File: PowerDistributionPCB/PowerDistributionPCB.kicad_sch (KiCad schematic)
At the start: 23 parts, among them J1 USB3_A

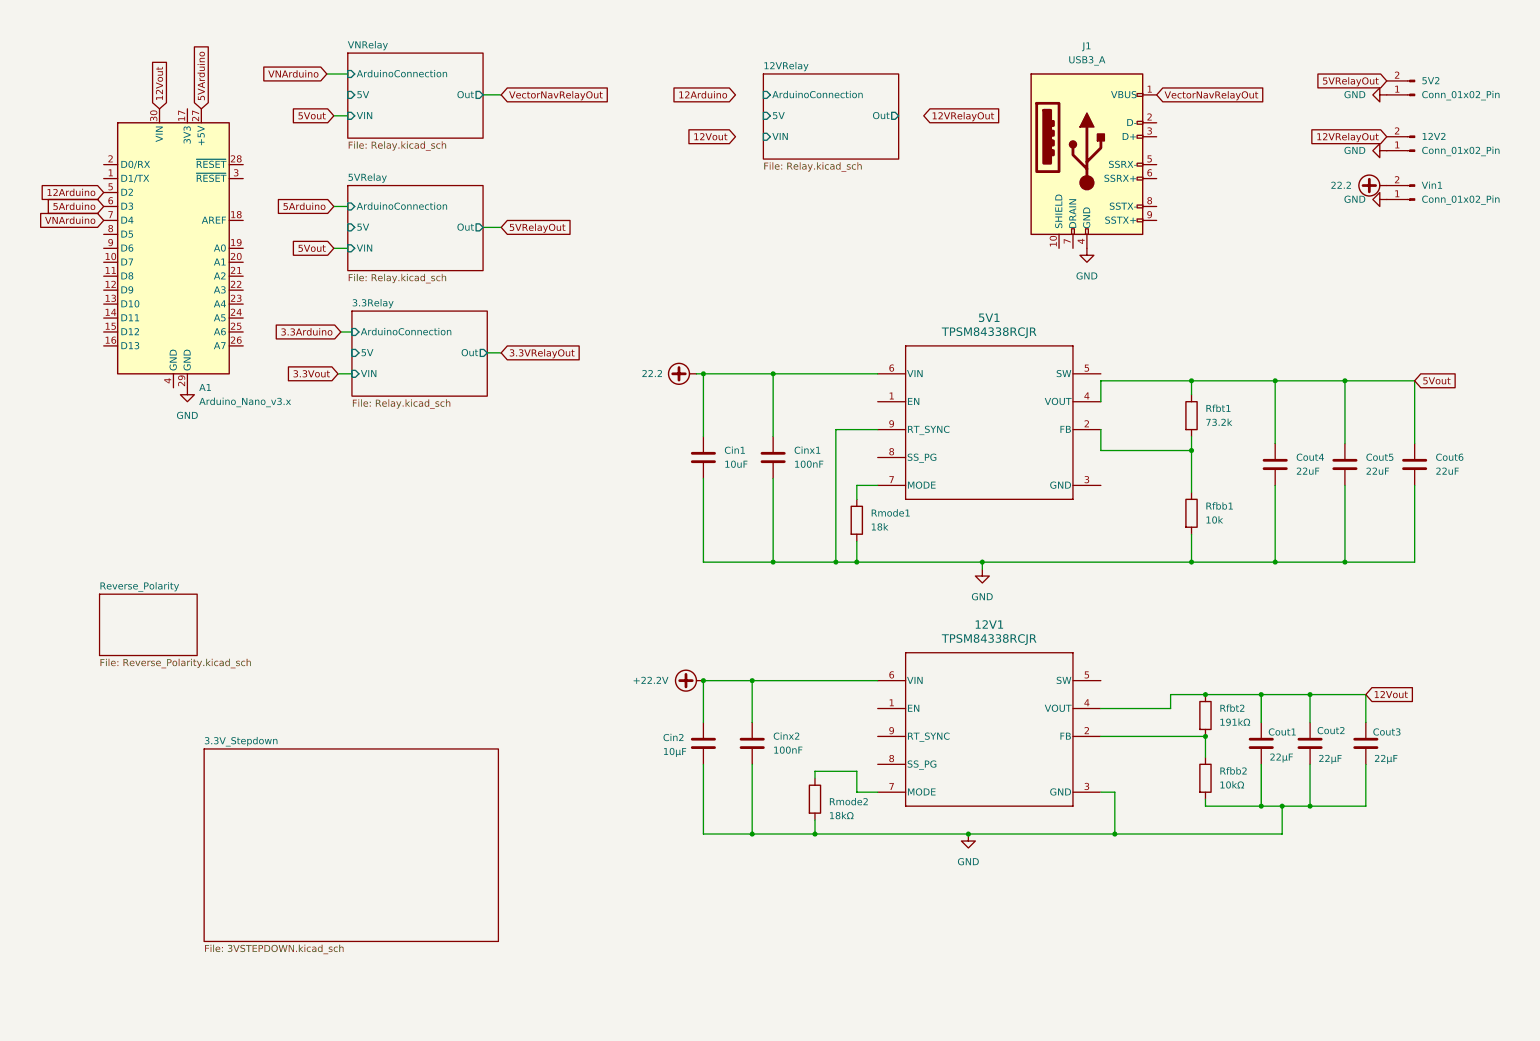
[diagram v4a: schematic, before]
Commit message: cleaned up relay work, somehow lost actual relay so will fix
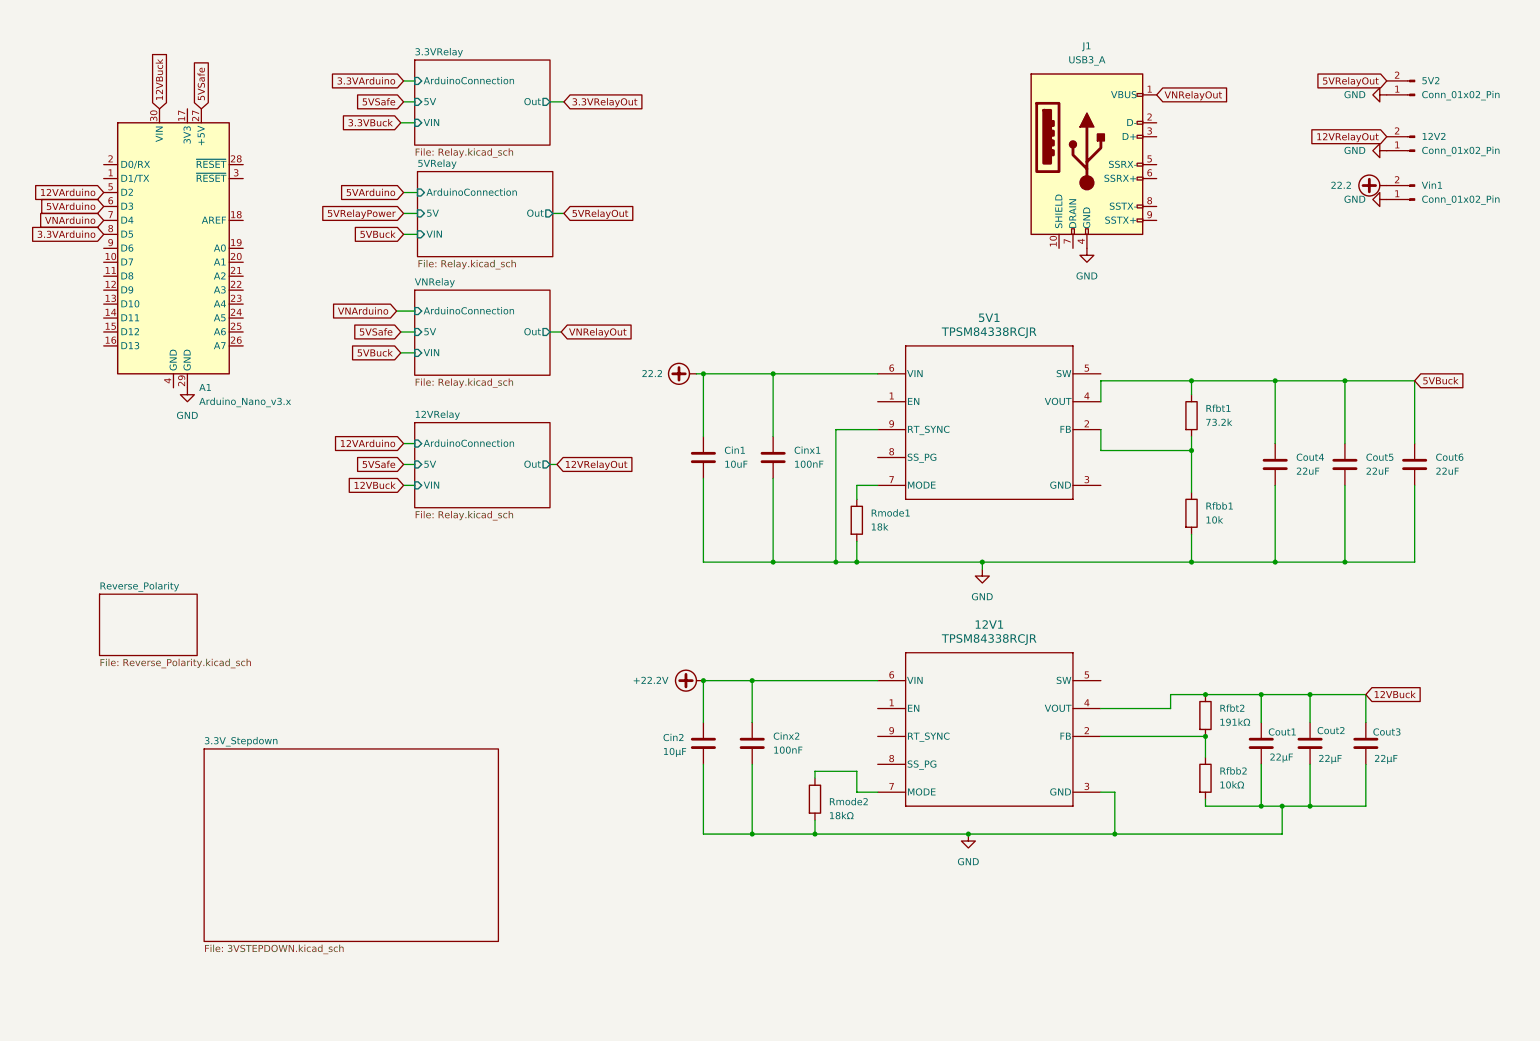
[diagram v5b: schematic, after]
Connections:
- net 5Arduino is gone; now on net 5VArduino: A1.6 (D3)
- net 5VArduino: no longer A1.27 (+5V)
- net 3.3VArduino: now reaches A1.8 (D5)
- net 12Arduino renamed 12VArduino
- net 12Vout renamed 12VBuck
- net 5Vout renamed 5VBuck
- net VectorNavRelayOut renamed VNRelayOut
- new net 5VSafe: A1.27 (+5V)
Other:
- sheet 3.3Relay renamed 3.3VRelay

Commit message: adding things back to main sheet
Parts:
- added C? (x2): 22µF, symbol Device:C
- added C?: 0.1µF, symbol Device:C
- added C?: 10µF, symbol Device:C
- added D?: MMSZ5242BS-7-F, symbol Device:D_Zener
- added L?: 4.7µH, symbol Device:L
- added Q1: AOD4185, TO252_AOS, symbol CU_Sail:AOD4185
- added R? (x2): 10k, symbol Device:R
- added R? (x2): 100k, symbol Device:R
- added U?: AP63203WU, Package_TO_SOT_SMD:TSOT-23-6, symbol Regulator_Switching:AP63203WU
- renumbered Cinx1 to Cin2
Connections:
- net 3.3VBuck: now also C?.1, C?.1, L?.2, U?.1 (FB)
- net GND: now also 5V1.3 (GND), C?.2, C?.2, C?.2, R?.1, R?.2, U?.4 (GND)
- net +22.2V renamed Sys_Vin
- net Sys_Vin: now also 5V1.6 (VIN), Cin1.1, Cin2.1, C?.1, Q1.2 (D), R?.2, U?.3 (IN)
- removed net 22.2: 5V1.6 (VIN), Cin1.1, Cin2.1, Vin1.2 (Pin_2)
- new net: C?.2, L?.1, U?.5 (SW)
- new net: D?.2 (A), Q1.1 (G), R?.2, R?.2
- new net: R?.1, R?.1, U?.2 (EN)
- new net: C?.1, U?.6 (BST)
- new net Batt_Vin: D?.1 (K), Q1.3 (S), R?.1, Vin1.2 (Pin_2)
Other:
- removed sheet 3.3V_Stepdown
- removed sheet Reverse_Polarity
- moved on the sheet: 12V1, 5V1, Cin1, Cin2, Cinx2, Cout1, Cout2, Cout3, Cout4, Cout5, Cout6, J1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

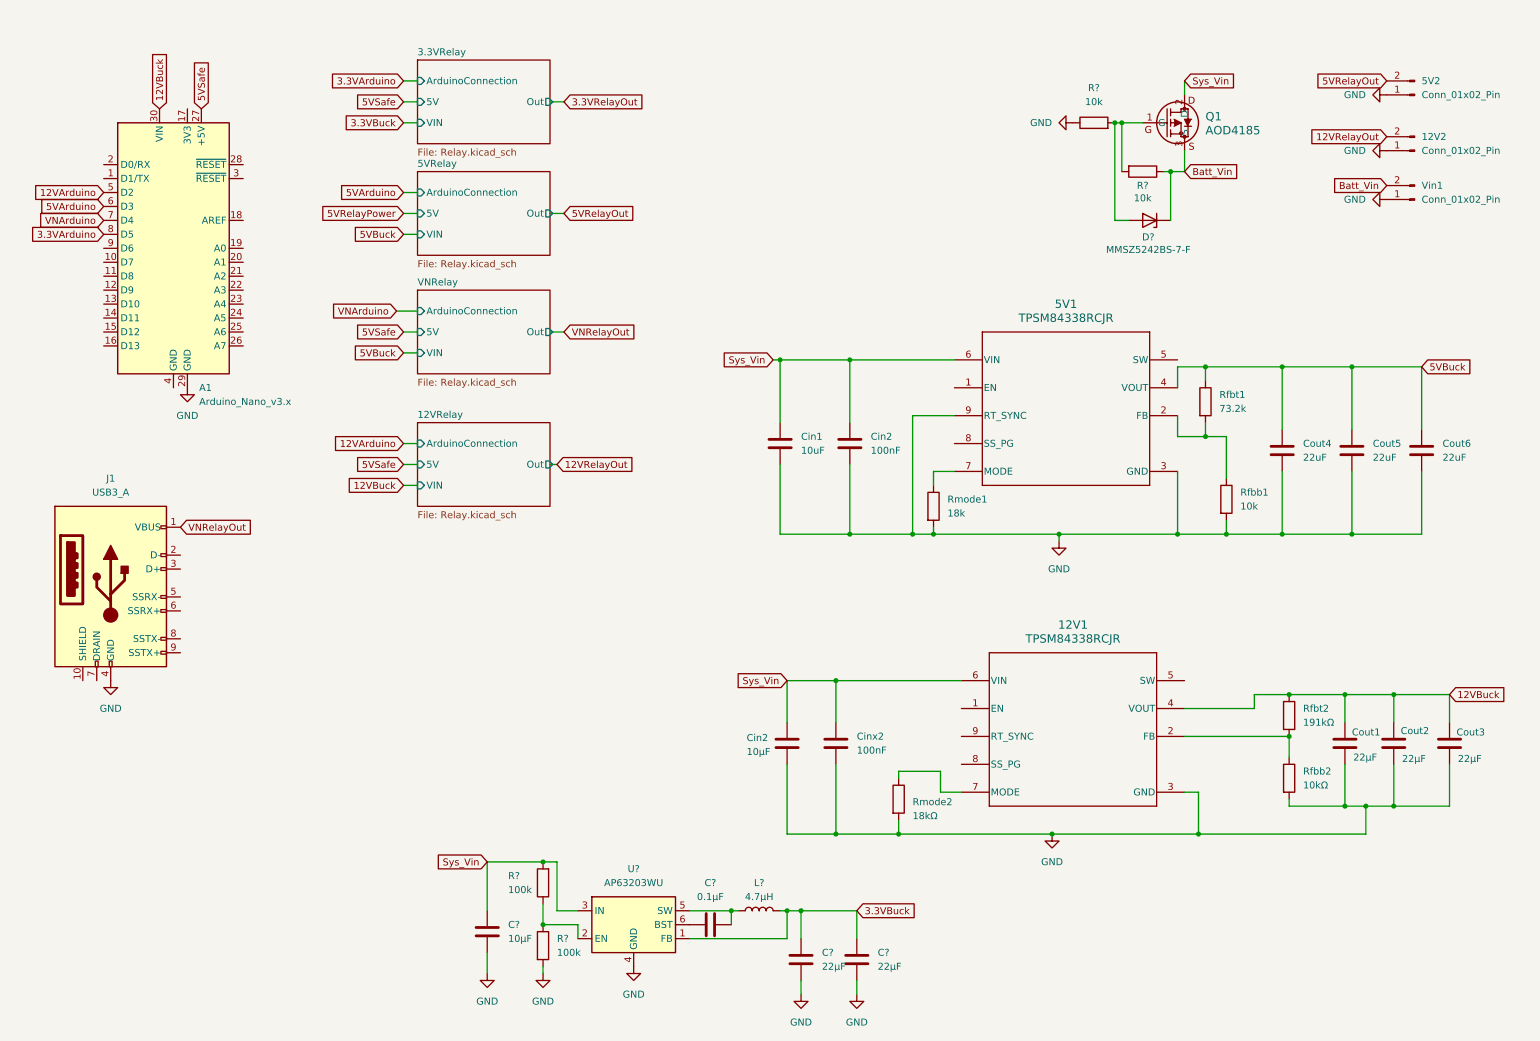
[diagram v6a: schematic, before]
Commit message: cleaned up main, updated labels
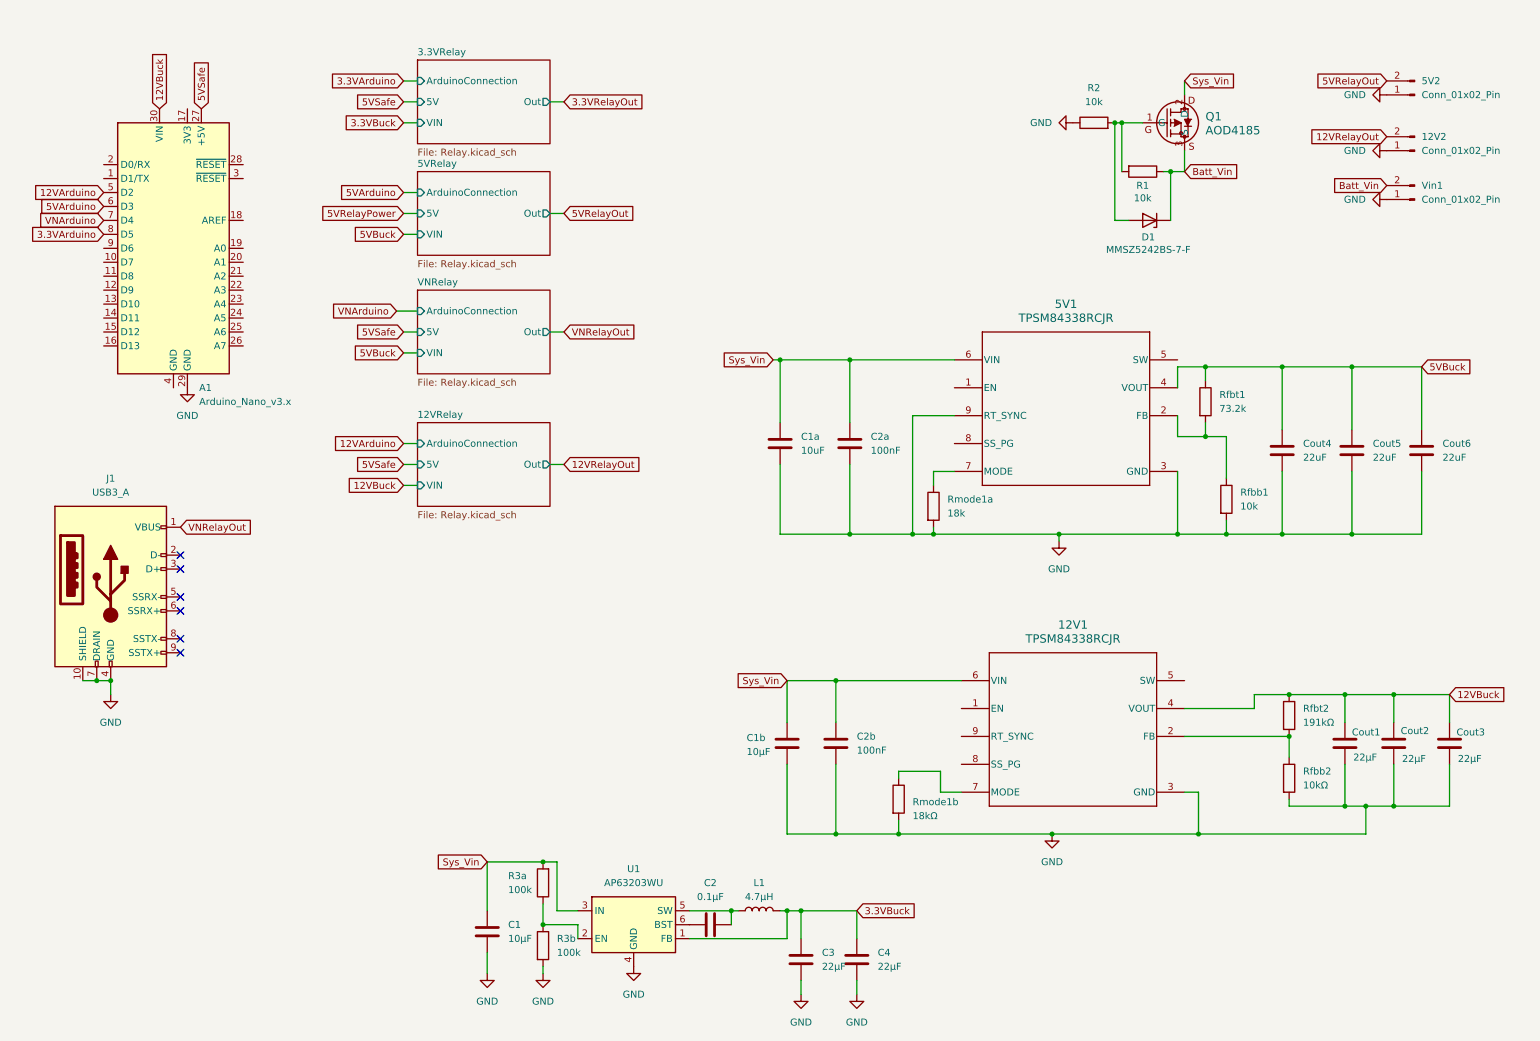
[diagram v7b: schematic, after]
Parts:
- gave numbers to parts that had none: 11
- renumbered Cin1 to C1a, Cin2 to C1b, Cin2 to C2a, Cinx2 to C2b, Rmode1 to Rmode1a, Rmode2 to Rmode1b
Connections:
- net GND: now also J1.10 (SHIELD), J1.7 (DRAIN)
- no-connect marks 0 -> 6
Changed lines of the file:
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@@
 	)
 	(junction
+		(at 27.94 129.54)
+		(diameter 0)
+		(color 0 0 0 0)
+	)
+	(junction
 		(at 261.62 132.08)
 		(diameter 0)
@@
 	)
 	(junction
+		(at 25.4 129.54)
+		(diameter 0)
+		(color 0 0 0 0)
+	)
+	(junction
 		(at 177.8 102.87)
 		(diameter 0)
@@
 		(color 0 0 0 0)
 	)
+	(no_connect
+		(at 40.64 116.84)
+	)
+	(no_connect
+		(at 40.64 109.22)
+	)
+	(no_connect
+		(at 40.64 106.68)
+	)
+	(no_connect
+		(at 40.64 124.46)
+	)
+	(no_connect
+		(at 40.64 114.3)
+	)
+	(no_connect
+		(at 40.64 121.92)
+	)
+	(wire
+		(pts
+			(xy 22.86 129.54) (xy 25.4 129.54)
+		)
+		(stroke
+			(width 0)
+			(type default)
+		)
+	)
 	(wire
 		(pts
@@
 	(wire
 		(pts
+			(xy 25.4 129.54) (xy 27.94 129.54)
+		)
+		(stroke
+			(width 0)
+			(type default)
+		)
+	)
+	(wire
+		(pts
 			(xy 236.22 132.08) (xy 242.57 132.08)
 		)
@@
 	(wire
 		(pts
+			(xy 27.94 132.08) (xy 27.94 129.54)
+		)
+		(stroke
+			(width 0)
+			(type default)
+		)
+	)
+	(wire
+		(pts
 			(xy 160.02 129.54) (xy 160.02 137.16)
 		)
@@
 	(wire
 		(pts
-			(xy 107.95 90.17) (xy 109.22 90.17)
+			(xy 107.95 90.17) (xy 110.49 90.17)
 		)
 		(stroke
@@
 	(global_label "12VRelayOut"
 		(shape input)
-		(at 109.22 90.17 0)
+		(at 110.49 90.17 0)
 		(fields_autoplaced yes)
 		(effects
@@
 		)
 		(property "Intersheetrefs" "${INTERSHEET_REFS}"
-			(at 124.0584 90.17 0)
+			(at 125.3284 90.17 0)
 			(effects
 				(font
@@
 		(dnp no)
 		(fields_autoplaced yes)
-		(property "Reference" "L?"
+		(property "Reference" "L1"
 			(at 146.05 166.37 90)
 			(effects
@@
 			(project "PowerDistributionPCB"
 				(path "/b27c75df-6223-4cc6-be69-062c2b02d5c6"
-					(reference "L?")
+					(reference "L1")
 					(unit 1)
 				)
@@
 		(on_board yes)
 		(dnp no)
-		(property "Reference" "Cin2"
+		(property "Reference" "C1b"
 			(at 143.764 139.954 0)
 			(effects
@@
 			(project ""
 				(path "/b27c75df-6223-4cc6-be69-062c2b02d5c6"
-					(reference "Cin2")
+					(reference "C1b")
 					(unit 1)
 				)
@@
 		(dnp no)
 		(fields_autoplaced yes)
-		(property "Reference" "Cin1"
+		(property "Reference" "C1a"
 			(at 153.67 85.0899 0)
 			(effects
@@
 			(project "PowerDistributionPCB"
 				(path "/b27c75df-6223-4cc6-be69-062c2b02d5c6"
-					(reference "Cin1")
+					(reference "C1a")
 					(unit 1)
 				)
@@
 		(on_board yes)
 		(dnp no)
-		(property "Reference" "R?"
+		(property "Reference" "R1"
 			(at 215.9 39.37 90)
 			(effects
@@
 			(project "PowerDistributionPCB"
 				(path "/b27c75df-6223-4cc6-be69-062c2b02d5c6"
-					(reference "R?")
+					(reference "R1")
 					(unit 1)
 				)
@@
 		(dnp no)
 		(fields_autoplaced yes)
-		(property "Reference" "C?"
+		(property "Reference" "C4"
 			(at 167.64 179.0699 0)
 			(effects
@@
 			(project "PowerDistributionPCB"
 				(path "/b27c75df-6223-4cc6-be69-062c2b02d5c6"
-					(reference "C?")
+					(reference "C4")
 					(unit 1)
 				)
@@
 		(on_board yes)
 		(dnp no)
-		(property "Reference" "Rmode2"
+		(property "Reference" "Rmode1b"
 			(at 173.99 151.638 0)
 			(effects
@@
 			(project ""
 				(path "/b27c75df-6223-4cc6-be69-062c2b02d5c6"
-					(reference "Rmode2")
+					(reference "Rmode1b")
 					(unit 1)
 				)
@@
 		(dnp no)
 		(fields_autoplaced yes)
-		(property "Reference" "Cinx2"
+		(property "Reference" "C2b"
 			(at 163.83 139.6999 0)
 			(effects
@@
 			(project ""
 				(path "/b27c75df-6223-4cc6-be69-062c2b02d5c6"
-					(reference "Cinx2")
+					(reference "C2b")
 					(unit 1)
 				)
@@
 		(dnp no)
 		(fields_autoplaced yes)
-		(property "Reference" "U?"
+		(property "Reference" "U1"
 			(at 123.19 163.83 0)
 			(effects
@@
 			(project "PowerDistributionPCB"
 				(path "/b27c75df-6223-4cc6-be69-062c2b02d5c6"
-					(reference "U?")
+					(reference "U1")
 					(unit 1)
 				)
@@
 		(on_board yes)
 		(dnp no)
-		(property "Reference" "D?"
+		(property "Reference" "D1"
 			(at 216.916 48.768 0)
 			(effects
@@
 			(project "PowerDistributionPCB"
 				(path "/b27c75df-6223-4cc6-be69-062c2b02d5c6"
-					(reference "D?")
+					(reference "D1")
 					(unit 1)
 				)
@@
 		(dnp no)
 		(fields_autoplaced yes)
-		(property "Reference" "R?"
+		(property "Reference" "R2"
 			(at 207.01 21.59 90)
 			(effects
@@
 			(project "PowerDistributionPCB"
 				(path "/b27c75df-6223-4cc6-be69-062c2b02d5c6"
-					(reference "R?")
+					(reference "R2")
 					(unit 1)
 				)
@@
 		(on_board yes)
 		(dnp no)
-		(property "Reference" "R?"
+		(property "Reference" "R3a"
 			(at 100.33 165.1 0)
 			(effects
@@
 			(project "PowerDistributionPCB"
 				(path "/b27c75df-6223-4cc6-be69-062c2b02d5c6"
-					(reference "R?")
+					(reference "R3a")
 					(unit 1)
 				)
@@
 		(dnp no)
 		(fields_autoplaced yes)
-		(property "Reference" "C?"
+		(property "Reference" "C2"
 			(at 137.16 166.37 90)
 			(effects
@@
 			(project "PowerDistributionPCB"
 				(path "/b27c75df-6223-4cc6-be69-062c2b02d5c6"
-					(reference "C?")
+					(reference "C2")
 					(unit 1)
 				)
@@
 		(dnp no)
 		(fields_autoplaced yes)
-		(property "Reference" "R?"
+		(property "Reference" "R3b"
 			(at 109.22 176.5299 0)
 			(effects
@@
 			(project "PowerDistributionPCB"
 				(path "/b27c75df-6223-4cc6-be69-062c2b02d5c6"
-					(reference "R?")
+					(reference "R3b")
 					(unit 1)
 				)
@@
 	(symbol
 		(lib_id "power:GND")
-		(at 27.94 129.54 0)
+		(at 27.94 132.08 0)
 		(unit 1)
 		(exclude_from_sim no)
@@
 		(fields_autoplaced yes)
 		(property "Reference" "#PWR011"
-			(at 27.94 135.89 0)
+			(at 27.94 138.43 0)
 			(effects
 				(font
@@
 		)
 		(property "Value" "GND"
-			(at 27.94 134.62 0)
+			(at 27.94 137.16 0)
 			(effects
 				(font
@@
 		)
 		(property "Footprint" ""
-			(at 27.94 129.54 0)
+			(at 27.94 132.08 0)
 			(effects
 				(font
@@
 		)
 		(property "Datasheet" ""
-			(at 27.94 129.54 0)
+			(at 27.94 132.08 0)
 			(effects
 				(font
@@
 		)
 		(property "Description" "Power symbol creates a global label with name \"GND\" , ground"
-			(at 27.94 129.54 0)
+			(at 27.94 132.08 0)
 			(effects
 				(font
@@
 		(dnp no)
 		(fields_autoplaced yes)
-		(property "Reference" "C?"
+		(property "Reference" "C1"
 			(at 100.33 173.9899 0)
 			(effects
@@
 			(project "PowerDistributionPCB"
 				(path "/b27c75df-6223-4cc6-be69-062c2b02d5c6"
-					(reference "C?")
+					(reference "C1")
 					(unit 1)
 				)
@@
 		(on_board yes)
 		(dnp no)
-		(property "Reference" "C?"
+		(property "Reference" "C3"
 			(at 157.48 179.0699 0)
 			(effects
@@
 			(project "PowerDistributionPCB"
 				(path "/b27c75df-6223-4cc6-be69-062c2b02d5c6"
-					(reference "C?")
+					(reference "C3")
 					(unit 1)
 				)
@@
 		(dnp no)
 		(fields_autoplaced yes)
-		(property "Reference" "Rmode1"
+		(property "Reference" "Rmode1a"
 			(at 180.34 96.5199 0)
 			(effects
@@
 			(project "PowerDistributionPCB"
 				(path "/b27c75df-6223-4cc6-be69-062c2b02d5c6"
-					(reference "Rmode1")
+					(reference "Rmode1a")
 					(unit 1)
 				)
@@
 		(dnp no)
 		(fields_autoplaced yes)
-		(property "Reference" "Cin2"
+		(property "Reference" "C2a"
 			(at 166.37 85.0899 0)
 			(effects
@@
 			(project "PowerDistributionPCB"
 				(path "/b27c75df-6223-4cc6-be69-062c2b02d5c6"
-					(reference "Cin2")
+					(reference "C2a")
 					(unit 1)
 				)
@@
 		)
 		(pin "Out" output
-			(at 108.458 24.13 0)
+			(at 107.95 24.13 0)
 			(effects
 				(font
@@
 		)
 		(pin "Out" output
-			(at 108.458 44.45 0)
+			(at 107.95 44.45 0)
 			(effects
 				(font
@@
 		)
 		(pin "Out" output
-			(at 108.458 66.04 0)
+			(at 107.95 66.04 0)
 			(effects
 				(font
@@
 		)
 		(pin "Out" output
-			(at 108.458 90.17 0)
+			(at 107.95 90.17 0)
 			(effects
 				(font
